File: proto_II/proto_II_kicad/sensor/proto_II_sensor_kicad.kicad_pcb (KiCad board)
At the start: 2 copper layers, 15 x 15 mm, 18 parts, among them J1 Conn_01x02, J2 Conn_01x02, U1 XC6206P332MR, U2 BME280

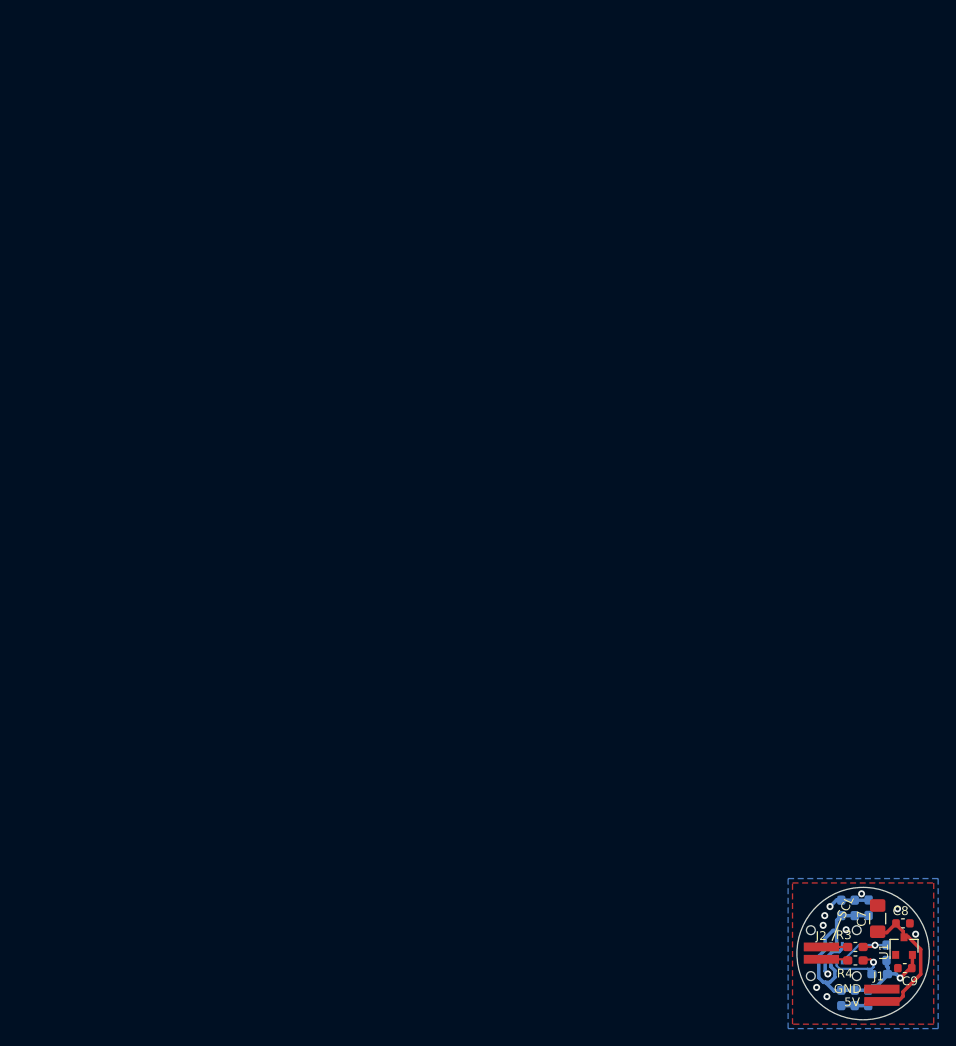
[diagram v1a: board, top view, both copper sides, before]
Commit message: Rework sensor board: allow hand-soldering of sensor
Additional sensor is used with easier footprint: Si70XX series
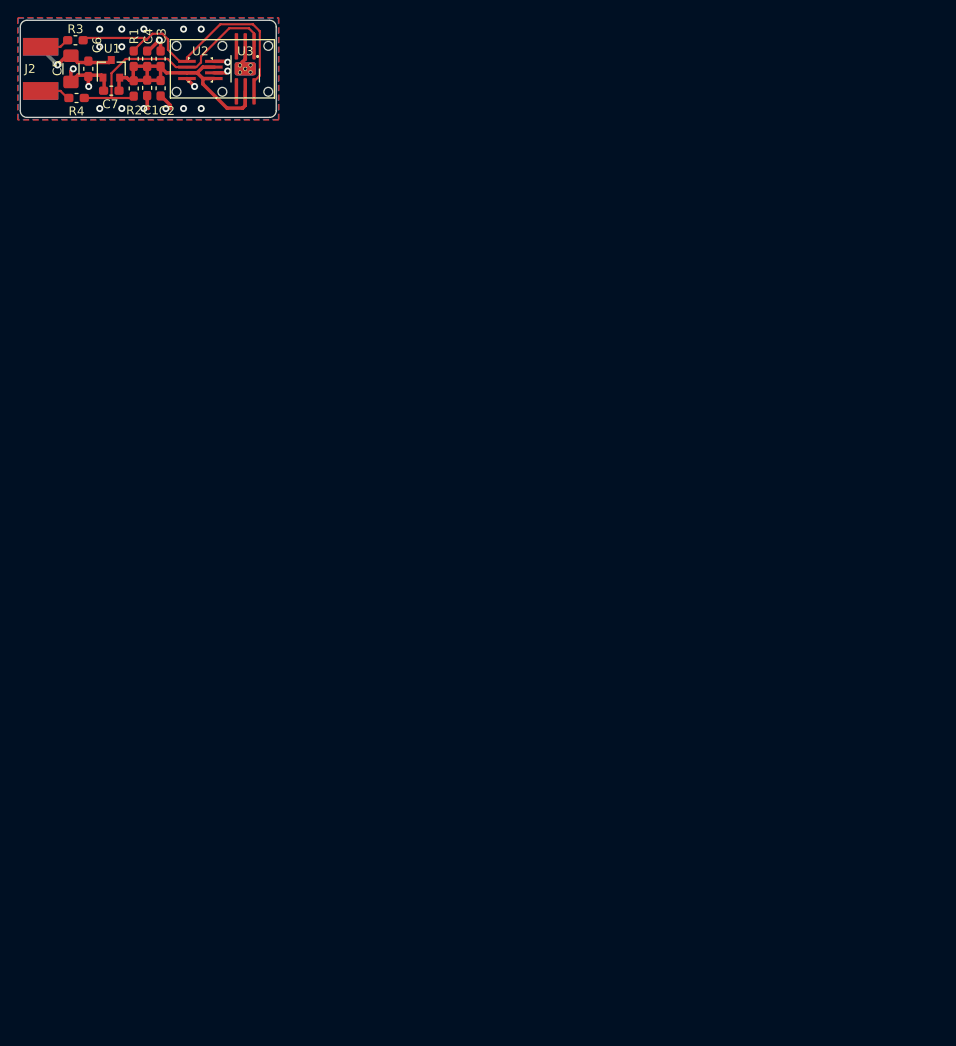
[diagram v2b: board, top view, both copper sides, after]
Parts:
- removed C8, C9: 1u, Capacitor_SMD:C_0603_1608Metric
- removed SF: SF2-CAP, Project:SENSIRION-SF2
- added REF**: SENSIRION-SF2-2PLACE, Project:SENSIRION-SF2-2PLACE, F.Cu at (58.4, 28.2)
- added U3: Si7020-A20, Project:DFN-6-1EP_3x3mm_P1mm_EP1.5x2.4mm_HandSoldering, F.Cu at (61.0, 28.2)
- C1: value 1u -> 100n; moved to F.Cu
- C2: value 100n -> 10n; moved to F.Cu
- C3, C6, R1, R2: moved to F.Cu
- C4: value 10n -> 100n; moved to F.Cu
- C5: value 100n -> 10u; footprint Capacitor_SMD:C_0603_1608Metric_Pad1.05x0.95mm_HandSolder -> Capacitor_SMD:C_1206_3216Metric_Pad1.42x1.75mm_HandSolder; moved to F.Cu
- C7: value 10u -> 1u; footprint Capacitor_SMD:C_1206_3216Metric_Pad1.42x1.75mm_HandSolder -> Capacitor_SMD:C_0603_1608Metric_Pad1.05x0.95mm_HandSolder
- J1: moved to B.Cu
- U2: footprint Package_LGA:Bosch_LGA-8_2.5x2.5mm_P0.65mm_ClockwisePinNumbering -> Project:Bosch_LGA-8_2.5x2.5mm_P0.65mm_ClockwisePinNumbering_HandSoldering; moved to F.Cu
- moved J1 141.8 mm to (37.8, 28.2), turned to 270 degrees
- moved C5 137.7 mm to (41.2, 28.2)
- moved C6 137.4 mm to (43.2, 28.2)
- moved R3 135.5 mm to (41.7, 25.0)
- moved U1 134.0 mm to (45.8, 28.2)
- moved J2 133.7 mm to (37.8, 28.2)
- moved R1 132.4 mm to (48.4, 27.1)
- moved C4 132.3 mm to (49.9, 27.1), turned to 90 degrees
- moved R4 131.7 mm to (41.9, 31.6)
- moved R2 131.2 mm to (48.4, 30.5), turned to 270 degrees
- moved C7 127.8 mm to (45.8, 30.7), turned to 180 degrees
- moved C1 123.7 mm to (49.9, 30.4), turned to 270 degrees
- moved C3 123.3 mm to (51.4, 27.1)
- moved U2 123.1 mm to (55.9, 28.4), turned to 90 degrees
- moved C2 121.7 mm to (51.4, 30.4), turned to 270 degrees
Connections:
- net Net-(R1-Pad2) renamed /SCL_IC
- net Net-(R2-Pad2) renamed /SDA_IC
- C5 pad 1: +3V3 -> +5V
- C6 pad 1: +3V3 -> +5V
- C7 pad 1: +5V -> +3V3
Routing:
- net /SCL_IC: track 7.16 -> 32.6 mm, vias 1 -> 0
- net /SDA_IC: track 7.41 -> 29.6 mm, vias 1 -> 0
- net GND: track 13.5 -> 21.9 mm, vias 10 -> 19
- net +5V: track 15.9 -> 9.57 mm, vias 0 -> 1
- net /SDA: track 2.99 -> 3.64 mm
- net +3V3: track 32.1 -> 31.7 mm, vias 1 -> 0
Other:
- board size 15 x 15 mm -> 29 x 11 mm
- board text added: "GX connector"
- board text removed: "5V"
- board text removed: "GND"
- board text removed: "SCL"
